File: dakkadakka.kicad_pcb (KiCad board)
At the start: 2 copper layers, 228.6 x 57.2 mm, 75 parts

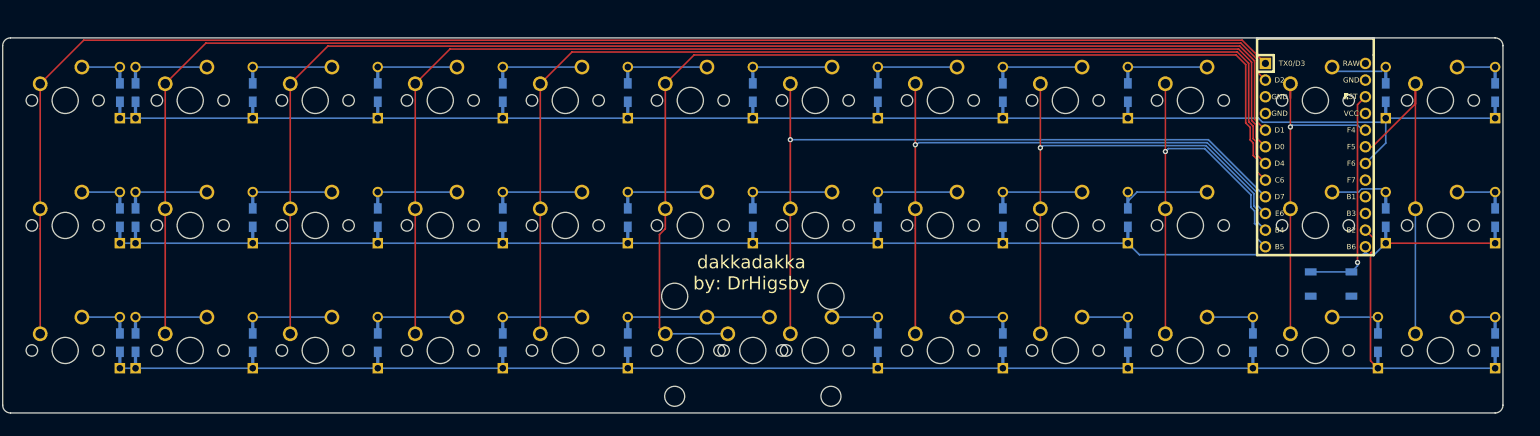
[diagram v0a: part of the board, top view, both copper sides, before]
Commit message: Reversible PCB update
Reversible PCB update
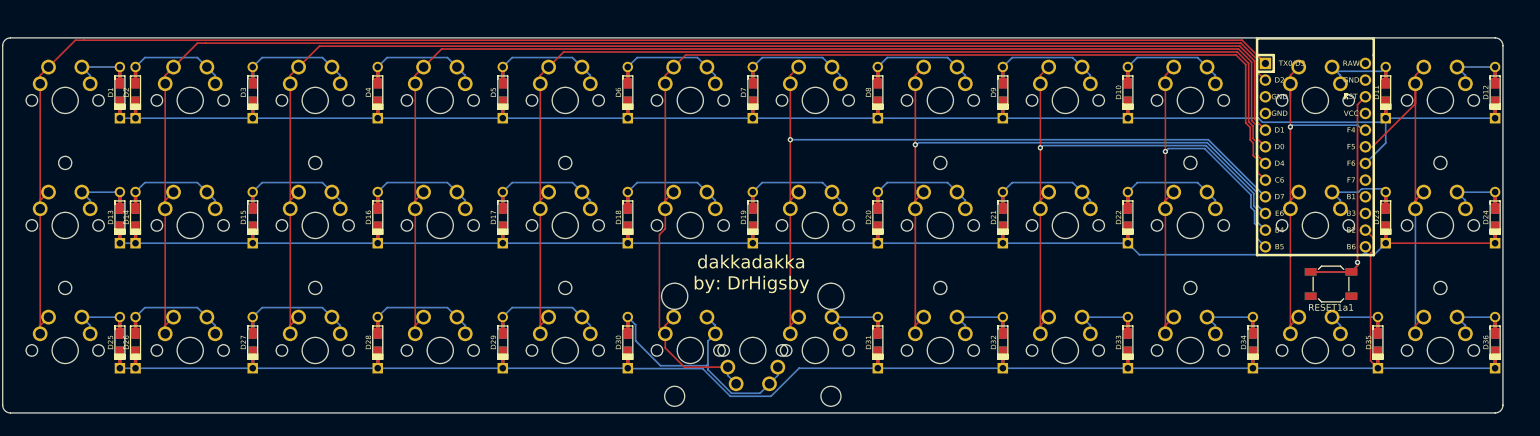
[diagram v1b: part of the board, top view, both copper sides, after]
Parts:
- added RESET1a1: SW_Push, Button_Switch_SMD:SW_SPST_SKQG_WithoutStem, F.Cu at (242.9, 78.0)
- D1, D10, D11, D12, D13, D14, D15, D16, D17, D18, D19, D2, D20, D21, D22, D23, D24, D25, D26, D27, D28, D29, D3, D30, D31, D32, D33, D34, D35, D36, D4, D5, D6, D7, D8, D9: footprint Keebio-Parts:Diode-Hybrid-Back -> Keebio-Parts:Diode-dual
- MX1, MX10, MX11, MX12, MX13, MX14, MX15, MX16, MX17, MX18, MX19, MX2, MX20, MX21, MX22, MX23, MX24, MX25, MX26, MX27, MX28, MX29, MX3, MX30, MX31, MX32, MX33, MX34, MX35, MX36, MX4, MX5, MX6, MX7, MX8, MX9: footprint MX_Only:MXOnly-1U-NoLED -> MX_Only:MX_ONLY_1u_NOLED_REVERSIBLE
- MX30a1: footprint MX_Only:MXOnly-2U-ReversedStabilizers-NoLED -> MX_Only:MXOnly-2U-NoLED-REVERSIBLE
- turned MX30a1 to 180 degrees
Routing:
- net Net-(D30-Pad2): track 21.6 -> 40.6 mm
- net C6: track 158.1 -> 171.4 mm
- net C11: track 52.1 -> 61.3 mm
- net C10: track 63.1 -> 72.3 mm
- net C9: track 80.1 -> 89.3 mm
- net C8: track 97.2 -> 106.4 mm
- net C7: track 114.1 -> 123.3 mm
- net C12: track 51.5 -> 60.7 mm
- net RST: track 33.8 -> 41.8 mm
- net C1: track 229.0 -> 235.9 mm
- net C5: track 165.1 -> 171.9 mm
- net C4: track 182.3 -> 189.2 mm
- net C2: track 211.7 -> 218.6 mm
- net C3: track 199.6 -> 206.4 mm
- net Net-(D9-Pad2): track 12.1 -> 16.3 mm
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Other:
- outline, holes or cut-outs redrawn
